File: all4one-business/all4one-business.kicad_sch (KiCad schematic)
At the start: 34 parts

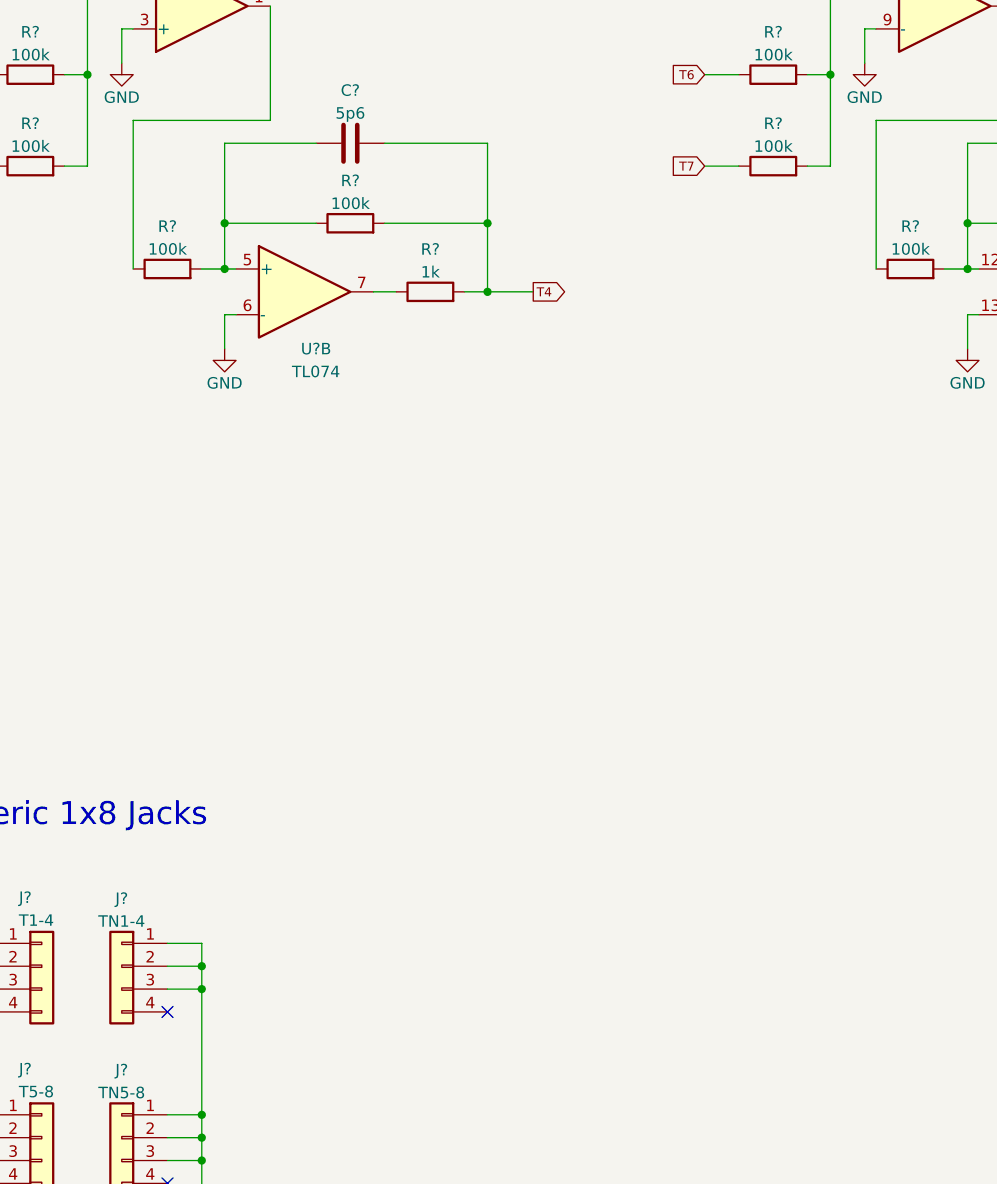
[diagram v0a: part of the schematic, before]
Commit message: :sparkles: all4one: Register upper output to second adder
Register T4 to TN4, so that all seven inputs are added if the upper
output is not populated.
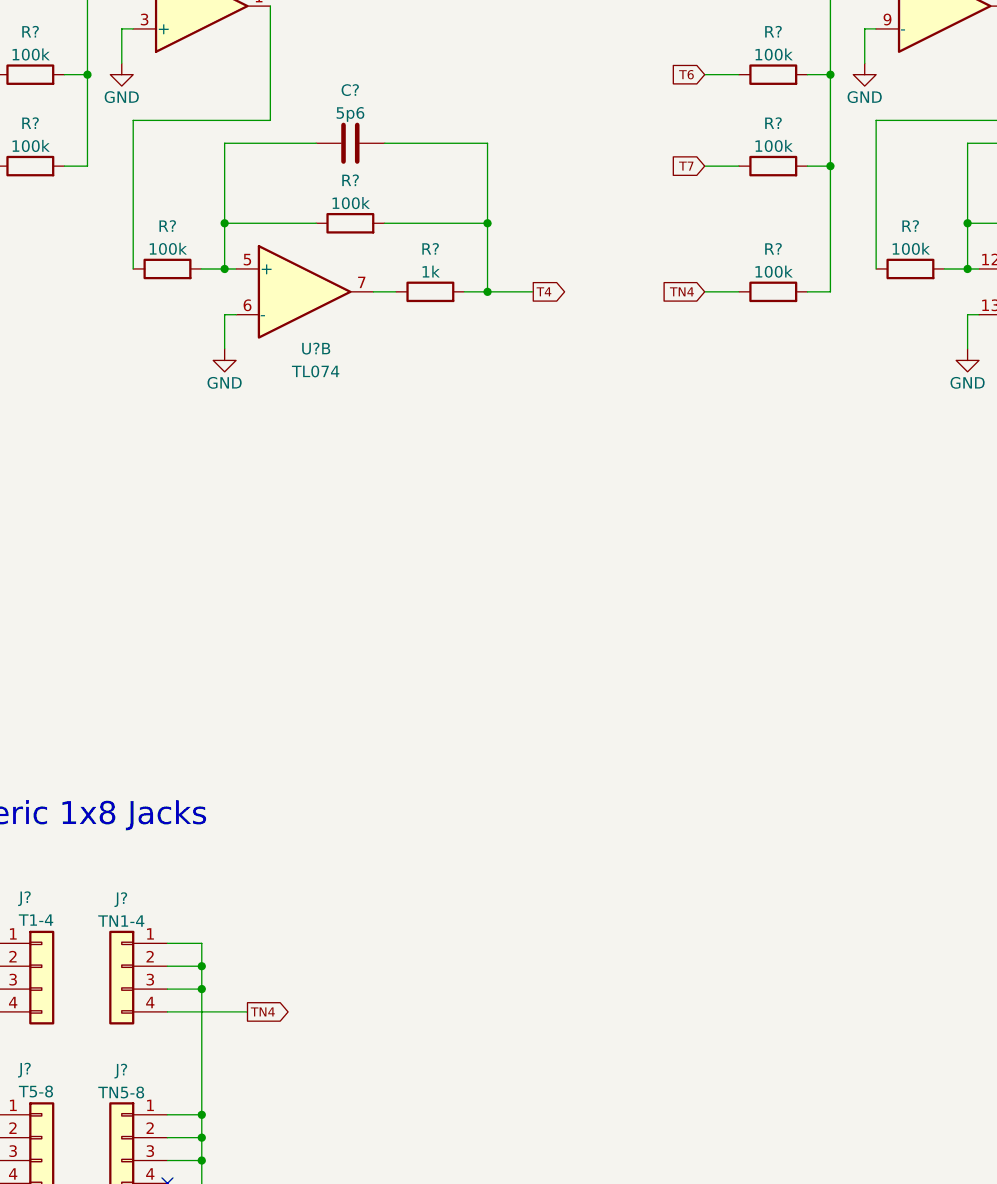
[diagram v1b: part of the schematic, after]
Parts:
- added R?: 100k, Resistor_THT:R_Axial_DIN0207_L6.3mm_D2.5mm_P7.62mm_Horizontal, symbol Device:R
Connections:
- net at R?.2, R?.2, R?.2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: now also R?.2
- net TN4: now reaches J?.4 (Pin_4)
- net TN4: now also R?.1
- no-connect marks 2 -> 1
